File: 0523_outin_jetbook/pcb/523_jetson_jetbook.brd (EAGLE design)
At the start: 101.6 x 55.9 mm, 60 parts, among them IC2 TXS0108

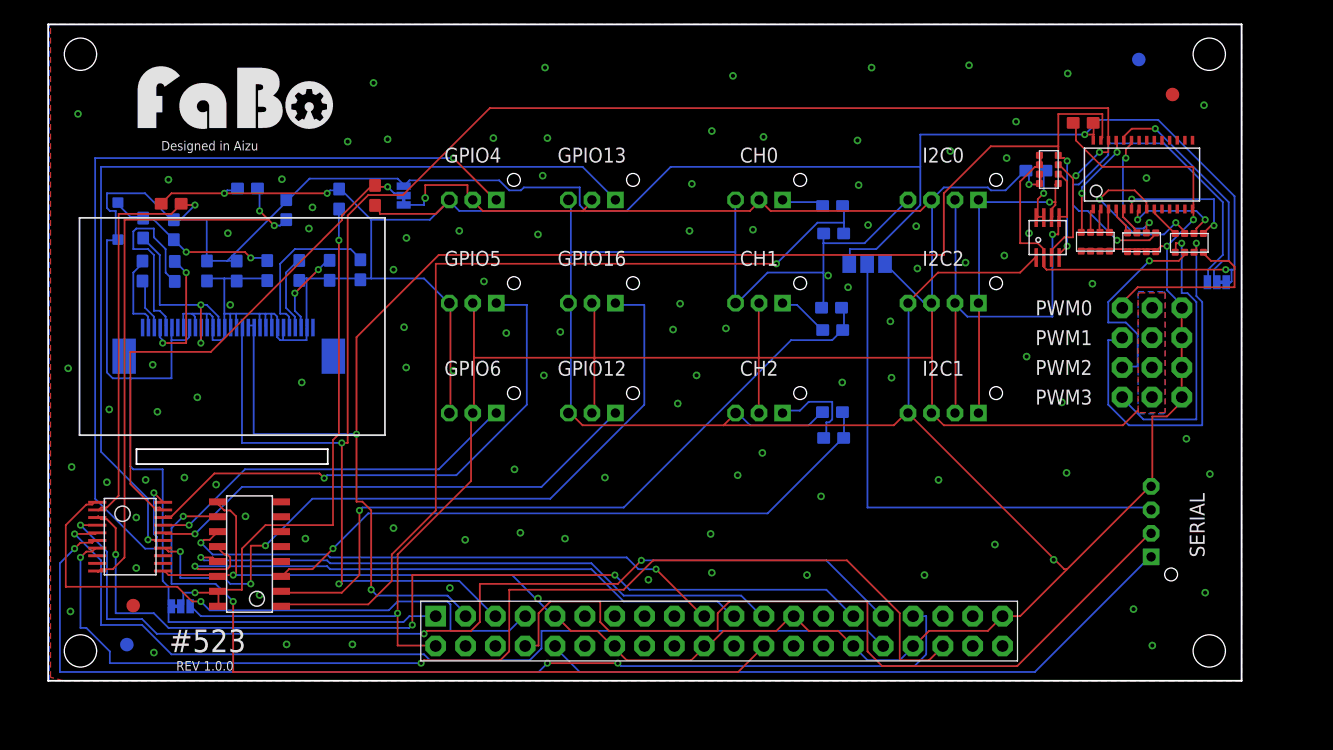
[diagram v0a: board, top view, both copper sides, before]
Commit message: CANの追加
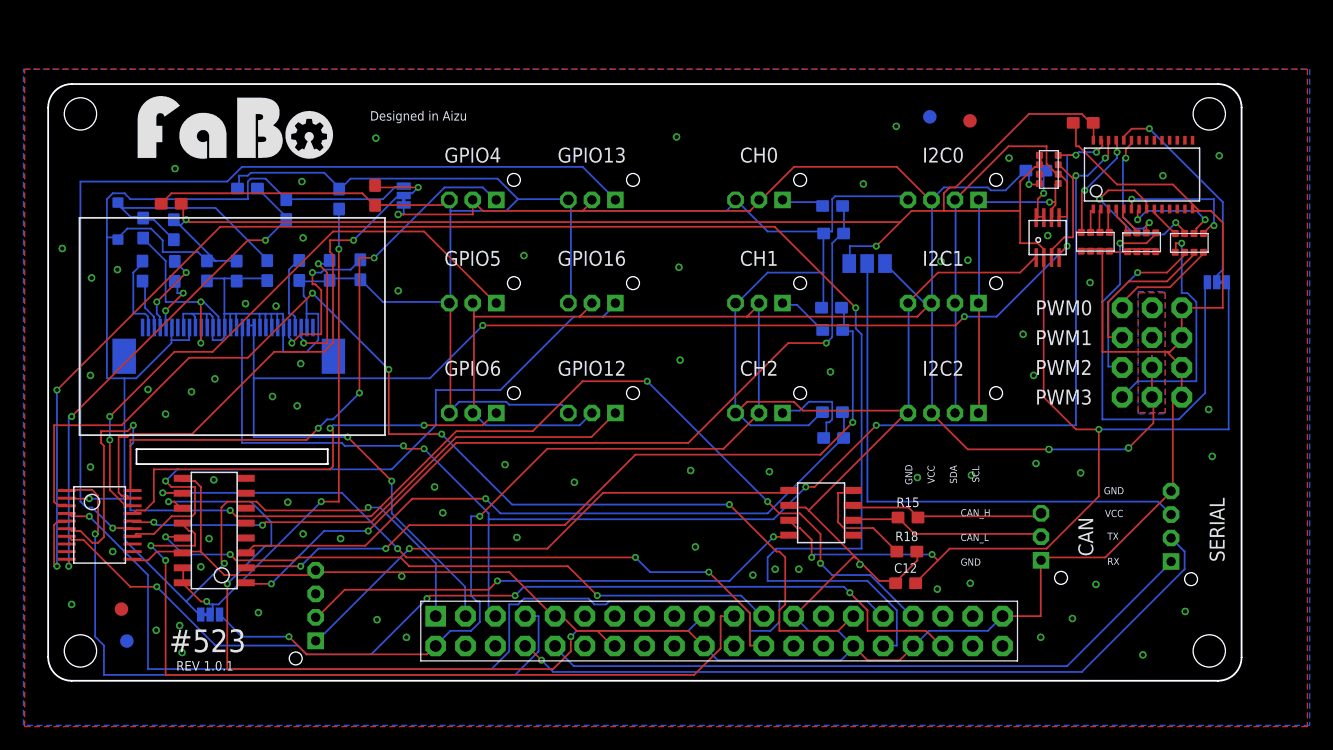
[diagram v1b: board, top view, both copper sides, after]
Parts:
- added C12: (no value), FaBo-Capacitor:0603
- added CAN: FABO_BRICK_CAN, FaBo-Template:FABO_BRICK_3PIN_B03B-PASK-1-CAN
- added JETSON: FABO_BRICK_CAN_4P, FaBo-Template:FABO_BRICK_CAN_B04B-PASL-1_BOTTOM
- added R15: 120, FaBo-Resistors:0603
- added R18: 10K, FaBo-Resistors:0603
- added U$8: SN65HVD230, FaBo-CAN:SN65HVD230
- moved U$6 18.4 mm to (75.1, 48.0)
- moved U$4 17.4 mm to (78.5, 47.7)
- moved I2C1 9.36 mm to (76.2, 32.1)
- moved I2C2 9.36 mm to (76.2, 22.8)
- moved IC3 3.61 mm to (14.1, 12.8)
- moved IC2 2.79 mm to (4.38, 13.3)
- moved SJ4 2.60 mm to (13.8, 5.64)
- moved U$7 2.54 mm to (15.2, 44.5)
- moved SERIAL 1.75 mm to (95.6, 13.2)
- moved U$3 1.04 mm to (6.24, 6.10)
- moved U$5 0.30 mm to (6.70, 3.38)
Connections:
- new net CRX: JETSON.CAN_RX, U$8.4
- new net CTX: JETSON.CAN_TX, U$8.1
- new net N$38: CAN.CAN_H, R15.2, U$8.7
- new net N$39: CAN.CAN_L, R15.1, U$8.6
- new net N$40: R18.1, U$8.8
- net 3V3: now also C12.2, U$8.3
- net GND: now also C12.1, CAN.GND, JETSON.GND, R18.2, U$8.2
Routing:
- net GND: track 418.2 -> 486.2 mm, vias 110 -> 75
- net GPIO12: track 80.9 -> 143.8 mm, vias 1 -> 3
- net 3V3: track 276.2 -> 327.1 mm, vias 3 -> 8
- net CTX: track 0.00 -> 45.7 mm, vias 0 -> 1
- net CRX: track 0.00 -> 43.2 mm, vias 0 -> 2
- net 5V: track 216.6 -> 250.3 mm, vias 3 -> 6
- net N$9: track 77.6 -> 51.7 mm, vias 2 -> 3
- net GPIO5: track 78.4 -> 100.5 mm, vias 3 -> 4
- net MOSI: track 47.3 -> 68.4 mm, vias 2 -> 3
- net SCL: track 151.1 -> 132.2 mm, vias 4 -> 6
- net PWM1: track 32.2 -> 13.3 mm, vias 1 -> 0
- net N$39: track 0.00 -> 17.0 mm
- net MISO: track 53.1 -> 69.8 mm, vias 1 -> 2
- net N$38: track 0.00 -> 16.7 mm
- net SDA: track 139.1 -> 126.0 mm, vias 4 -> 7
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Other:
- board size 101.6 x 55.9 mm -> 101.6 x 50.8 mm
- board text added: "GND"
- board text added: "REV 1.0.1"
- board text added: "RX"
- board text added: "SCL"
- board text added: "SDA"
- board text added: "TX"
- board text added: "VCC"
- board text removed: "F-519-1-9-A-N-J-0-P"
- board text removed: "REV 1.0.0"

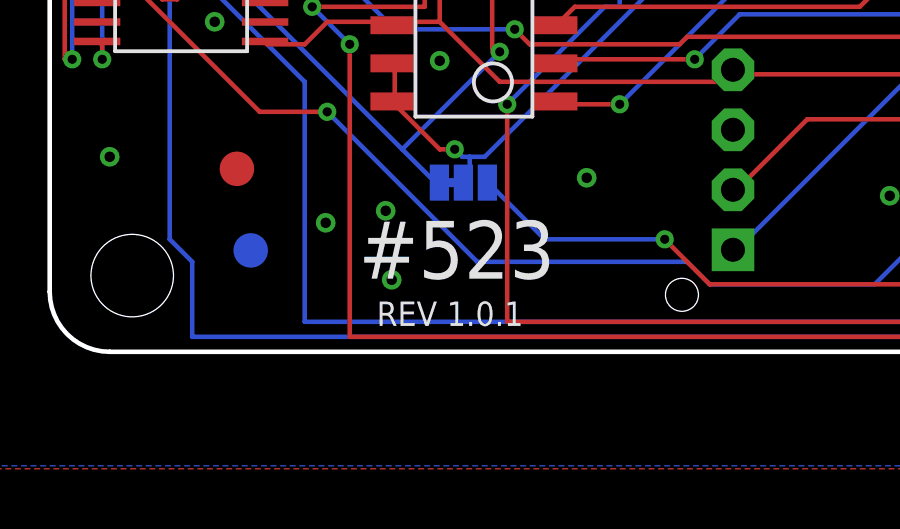
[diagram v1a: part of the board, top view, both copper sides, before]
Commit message: #523 Jetbook update 1.0.2 アナログ計測分圧4.7K,9.1Kの組み合わせで分圧。
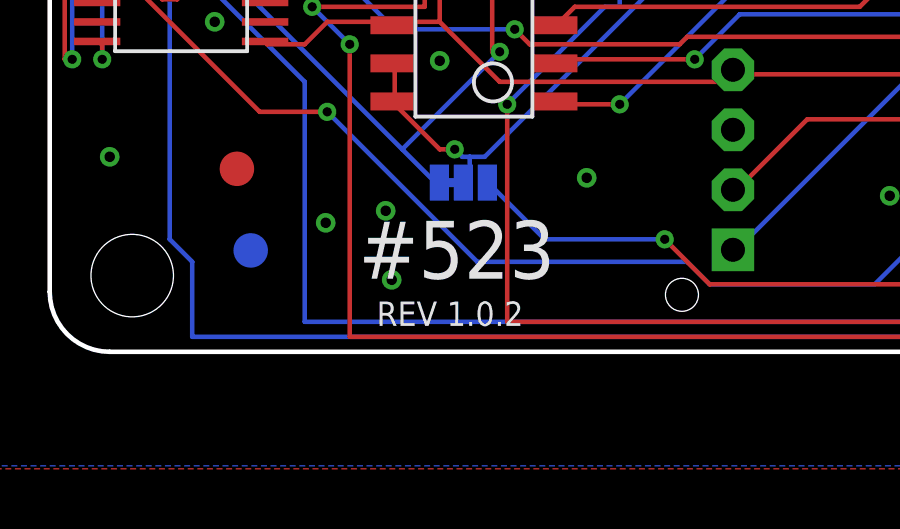
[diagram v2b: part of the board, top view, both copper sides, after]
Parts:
- R10, R14, R4: value 2.2K -> 4.7K
- R11, R12, R17: value 3.3K -> 9.1K
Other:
- board text added: "REV 1.0.2"
- board text removed: "REV 1.0.1"
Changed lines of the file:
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@@
 <?xml version="1.0" encoding="utf-8"?>
 <!DOCTYPE eagle SYSTEM "eagle.dtd">
-<eagle version="9.5.1">
+<eagle version="9.6.0">
 <drawing>
 <settings>
-<setting alwaysvectorfont="yes"/>
+<setting alwaysvectorfont="no"/>
 <setting keepoldvectorfont="yes"/>
 <setting verticaltext="up"/>
@@
 <board>
 <plain>
-<text x="13.343" y="1.676" size="0.8128" layer="21" font="vector" ratio="15" rot="R180" align="bottom-center">REV 1.0.1</text>
+<text x="13.343" y="1.676" size="0.8128" layer="21" font="vector" ratio="15" rot="R180" align="bottom-center">REV 1.0.2</text>
 <text x="10.298" y="2.436" size="1.9304" layer="21" font="vector" ratio="15">#523</text>
 <wire x1="7.52" y1="18.45" x2="23.8" y2="18.45" width="0.1524" layer="20"/>
@@
 </element>
 <element name="IC3" library="FaBo-ADC" package="MICROCHIP-MCP3008" value="" x="14.14" y="12.79" smashed="yes" rot="R90"/>
-<element name="R4" library="FaBo-Resistors" package="0603-BOTTOM" value="2.2K" x="66.78" y="40.42" smashed="yes">
+<element name="R4" library="FaBo-Resistors" package="0603-BOTTOM" value="4.7K" x="66.78" y="40.42" smashed="yes">
 <attribute name="VALUE" x="66.68" y="39.62" size="0.8128" layer="28" font="vector" ratio="12" align="center"/>
 </element>
-<element name="R10" library="FaBo-Resistors" package="0603-BOTTOM" value="2.2K" x="66.79" y="29.86" smashed="yes">
+<element name="R10" library="FaBo-Resistors" package="0603-BOTTOM" value="4.7K" x="66.79" y="29.86" smashed="yes">
 <attribute name="VALUE" x="66.19" y="28.76" size="0.8128" layer="28" font="vector" ratio="12" align="center"/>
 </element>
-<element name="R11" library="FaBo-Resistors" package="0603-BOTTOM" value="3.3K" x="66.87" y="38.08" smashed="yes">
+<element name="R11" library="FaBo-Resistors" package="0603-BOTTOM" value="9.1K" x="66.87" y="38.08" smashed="yes">
 <attribute name="VALUE" x="65.97" y="37.18" size="0.8128" layer="28" font="vector" ratio="12" align="center"/>
 </element>
-<element name="R12" library="FaBo-Resistors" package="0603-BOTTOM" value="3.3K" x="66.69" y="31.76" smashed="yes">
+<element name="R12" library="FaBo-Resistors" package="0603-BOTTOM" value="9.1K" x="66.69" y="31.76" smashed="yes">
 <attribute name="VALUE" x="66.99" y="31.76" size="0.8128" layer="28" font="vector" ratio="12" align="center"/>
 </element>
@@
 <attribute name="NAME" x="13.79" y="6.91" size="0.8128" layer="26" font="vector" ratio="12" rot="MR0" align="bottom-center"/>
 </element>
-<element name="R14" library="FaBo-Resistors" package="0603-BOTTOM" value="2.2K" x="66.87" y="20.67" smashed="yes">
+<element name="R14" library="FaBo-Resistors" package="0603-BOTTOM" value="4.7K" x="66.87" y="20.67" smashed="yes">
 <attribute name="VALUE" x="65.77" y="20.57" size="0.8128" layer="28" font="vector" ratio="12" align="center"/>
 </element>
-<element name="R17" library="FaBo-Resistors" package="0603-BOTTOM" value="3.3K" x="66.77" y="22.87" smashed="yes">
+<element name="R17" library="FaBo-Resistors" package="0603-BOTTOM" value="9.1K" x="66.77" y="22.87" smashed="yes">
 <attribute name="VALUE" x="66.97" y="22.07" size="0.8128" layer="28" font="vector" ratio="12" align="center"/>
 </element>

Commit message: #523 outin_jetbook　ロゴ修正
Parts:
- added LOGO1: (no value), component:LOGO_FABO_M
- U$7: value (none) -> LOGO_OSHW-M_BOTTOM; device FaBo-Logo:LOGO_FABO_L -> component:LOGO_OSHW_M_BOTTOM
- moved U$7 86.9 mm to (92.1, 3.81)
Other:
- board text added: "Jetson Jetbook"
- board text added: "Rev.1.0.2"
- board text removed: "REV 1.0.2"
